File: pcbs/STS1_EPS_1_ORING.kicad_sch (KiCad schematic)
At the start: 7 parts, among them U27 LTC4451AV#TRMPBF, U28 LTC4451AV#TRMPBF

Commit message: Fixed some warnings and errors.
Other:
- moved on the sheet: C7
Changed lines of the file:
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@@
 	(wire
 		(pts
-			(xy 49.53 113.03) (xy 49.53 114.935)
+			(xy 49.53 113.03) (xy 49.53 115.57)
 		)
 		(stroke
@@
 	(wire
 		(pts
-			(xy 49.53 122.555) (xy 49.53 125.73)
+			(xy 49.53 123.19) (xy 49.53 125.73)
 		)
 		(stroke
@@
 	(symbol
 		(lib_id "Device:C")
-		(at 49.53 118.745 0)
+		(at 49.53 119.38 0)
 		(unit 1)
 		(exclude_from_sim no)
@@
 		(dnp no)
 		(property "Reference" "C7"
-			(at 50.8 114.935 0)
+			(at 50.8 115.57 0)
 			(effects
 				(font
@@
 		)
 		(property "Value" "100n"
-			(at 50.8 122.555 0)
+			(at 50.8 123.19 0)
 			(effects
 				(font
@@
 		)
 		(property "Footprint" "Capacitor_SMD:C_0805_2012Metric"
-			(at 50.4952 122.555 0)
+			(at 50.4952 123.19 0)
 			(effects
 				(font
@@
 		)
 		(property "Datasheet" "~"
-			(at 49.53 118.745 0)
+			(at 49.53 119.38 0)
 			(effects
 				(font
@@
 		)
 		(property "Description" ""
-			(at 49.53 118.745 0)
+			(at 49.53 119.38 0)
 			(effects
 				(font
@@
 		)
 		(property "Value" "GND"
-			(at 52.07 62.2299 0)
-			(effects
-				(font
-					(size 1.27 1.27)
-				)
-				(justify left)
+			(at 49.53 66.04 0)
+			(effects
+				(font
+					(size 1.27 1.27)
+				)
 			)
 		)
@@
 			)
 		)
-		(property "Description" ""
+		(property "Description" "Power symbol creates a global label with name \"GND\" , ground"
 			(at 49.53 60.96 0)
 			(effects
@@
 			)
 		)
-		(property "Description" ""
+		(property "Description" "Power symbol creates a global label with name \"GND\" , ground"
 			(at 92.71 57.15 0)
 			(effects
@@
 			)
 		)
-		(property "Description" ""
+		(property "Description" "Power symbol creates a global label with name \"GND\" , ground"
 			(at 93.98 123.19 0)
 			(effects
@@
 			)
 		)
-		(property "Description" ""
+		(property "Description" "Power symbol creates a global label with name \"GND\" , ground"
 			(at 92.71 41.91 0)
 			(effects
@@
 		)
 		(property "Value" "GND"
-			(at 52.07 126.9999 0)
-			(effects
-				(font
-					(size 1.27 1.27)
-				)
-				(justify left)
+			(at 49.53 130.81 0)
+			(effects
+				(font
+					(size 1.27 1.27)
+				)
 			)
 		)
@@
 			)
 		)
-		(property "Description" ""
+		(property "Description" "Power symbol creates a global label with name \"GND\" , ground"
 			(at 49.53 125.73 0)
 			(effects
@@
 			)
 		)
-		(property "Description" ""
+		(property "Description" "Power symbol creates a global label with name \"GND\" , ground"
 			(at 102.87 144.78 0)
 			(effects
@@
 			)
 		)
-		(property "Description" ""
+		(property "Description" "Power symbol creates a global label with name \"GND\" , ground"
 			(at 93.98 107.95 0)
 			(effects

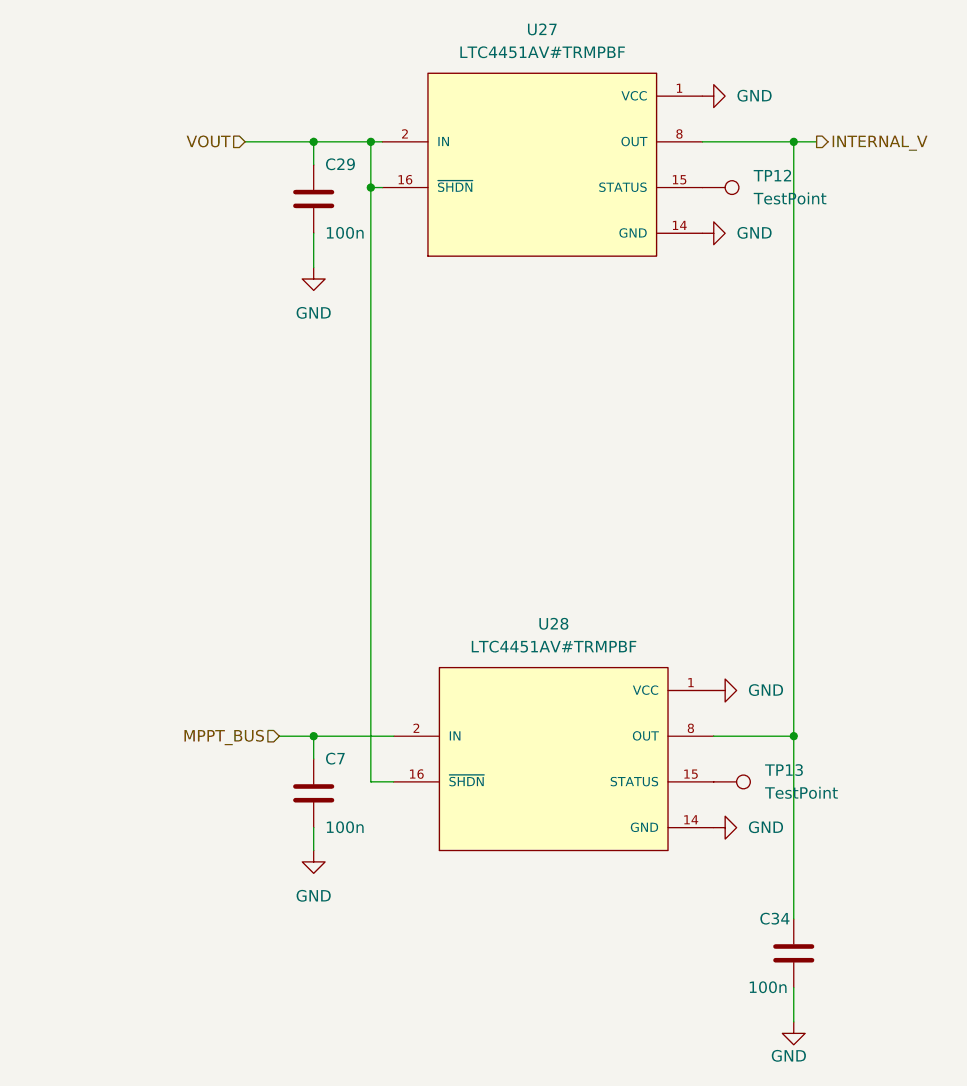
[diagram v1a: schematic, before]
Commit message: Separated the SHDN pins of the logic- and power oring. Also added TVS diodes to them, as this is recommended by the datasheet.
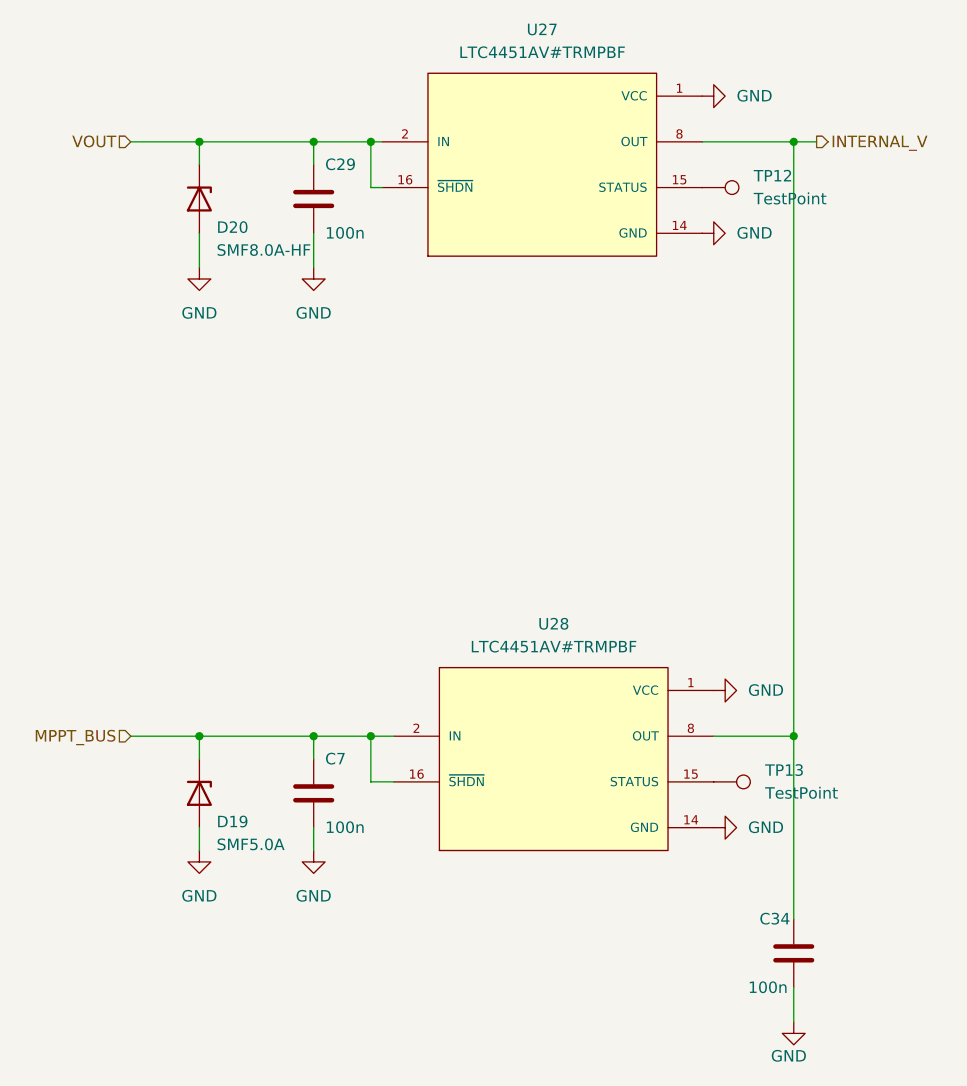
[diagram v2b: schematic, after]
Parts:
- added D19: SMF5.0A, Diode_SMD:D_SMF, symbol Device:D_Zener
- added D20: SMF8.0A-HF, Diode_SMD:D_SOD-123F, symbol Device:D_Zener
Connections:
- net GND: now also D19.2 (A), D20.2 (A)
- net MPPT_BUS: now also U28.16 (~{SHDN}), D19.1 (K)
- net VOUT: now also D20.1 (K); no longer U28.16 (~{SHDN})

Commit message: Started adding part numbers to passive components.
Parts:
- C29, C34, C7: Part Nr. (none) -> C0805T104K1RCLTU
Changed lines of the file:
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@@
+			)
+		)
+		(property "Part Nr." "C0805T104K1RCLTU"
+			(at 49.53 119.38 0)
+			(effects
+				(font
+					(size 1.27 1.27)
+				)
+				(hide yes)
 			)
 		)
@@
 			)
 		)
+		(property "Part Nr." "C0805T104K1RCLTU"
+			(at 49.53 53.34 0)
+			(effects
+				(font
+					(size 1.27 1.27)
+				)
+				(hide yes)
+			)
+		)
 		(pin "1"
 		)
@@
 			(at 102.87 137.16 0)
 			(effects
+				(font
+					(size 1.27 1.27)
+				)
+				(hide yes)
+			)
+		)
+		(property "Part Nr." "C0805T104K1RCLTU"
+			(at 102.87 137.16 0)
+			(effects
